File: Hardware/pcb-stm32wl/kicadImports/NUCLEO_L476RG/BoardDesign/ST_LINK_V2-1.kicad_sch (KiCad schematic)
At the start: 70 parts, among them CN1 5075BMR-05-SM, CN5 Header 6X1, CN6 Header 4, T2 9013, U12 STM32F103CBT6, U13 LD3985M33R, X1 8MHz(12pF)

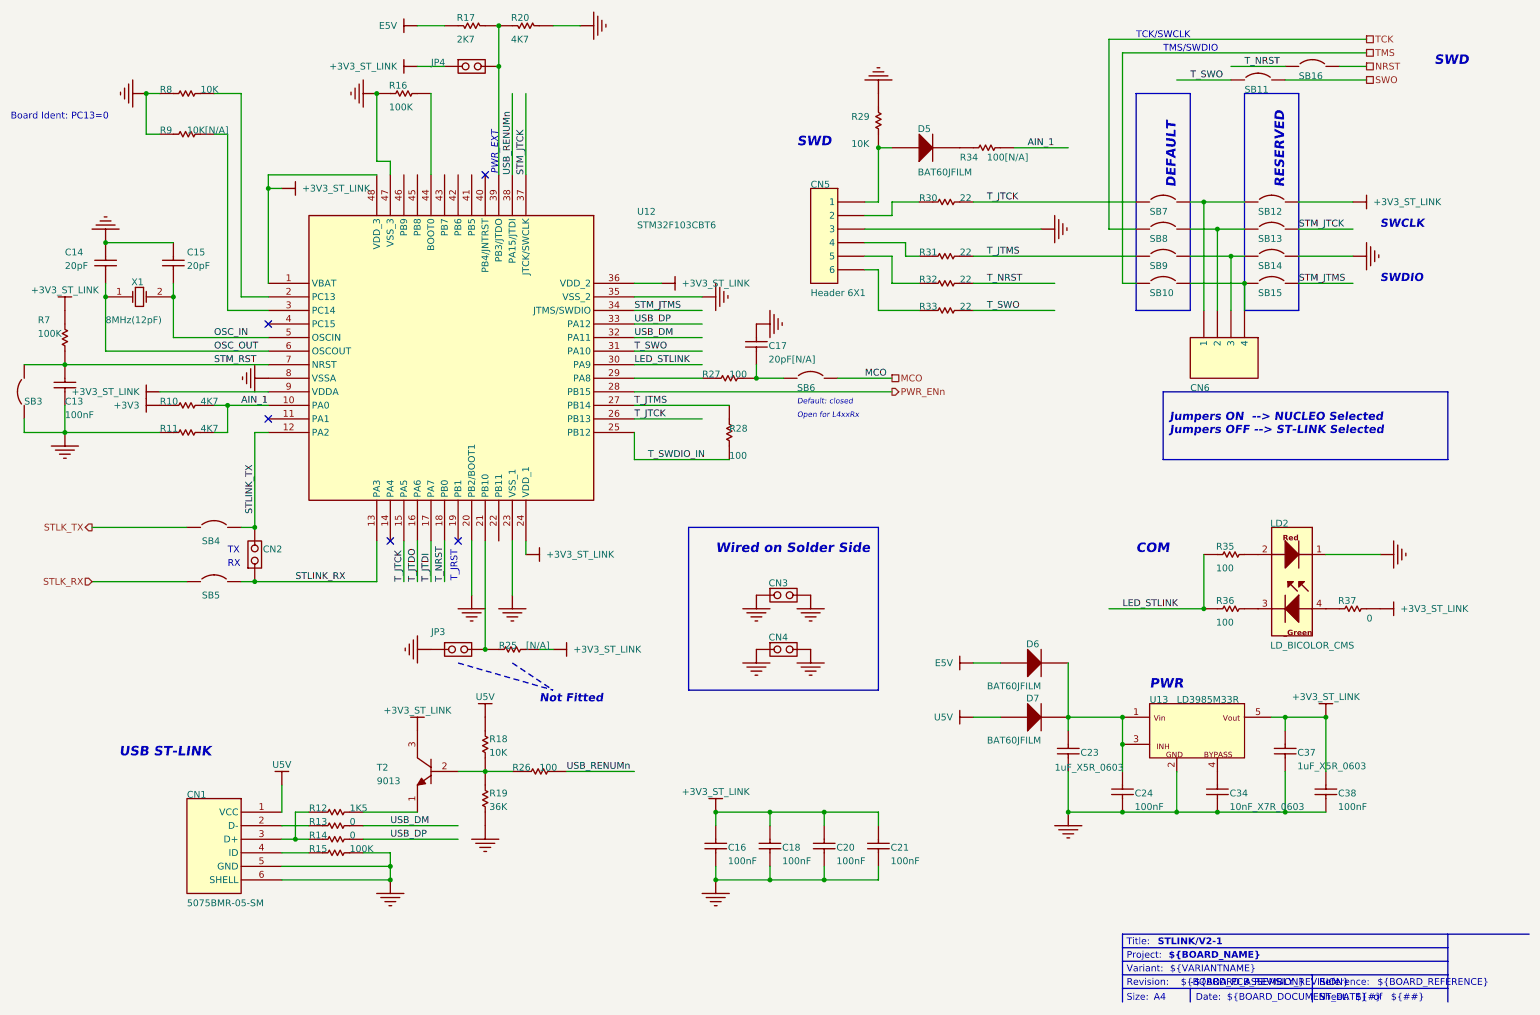
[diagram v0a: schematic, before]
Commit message: . Re-imported NUCLEO_L476RG/BoardDesign/* files using KiCad 9.0.0 one at a time (to avoid a bug evident in misconnections in MCU_64), copied the schematic contents into local kicad_sch files with the same names, prefixed with NUCLEO_L476RG_*
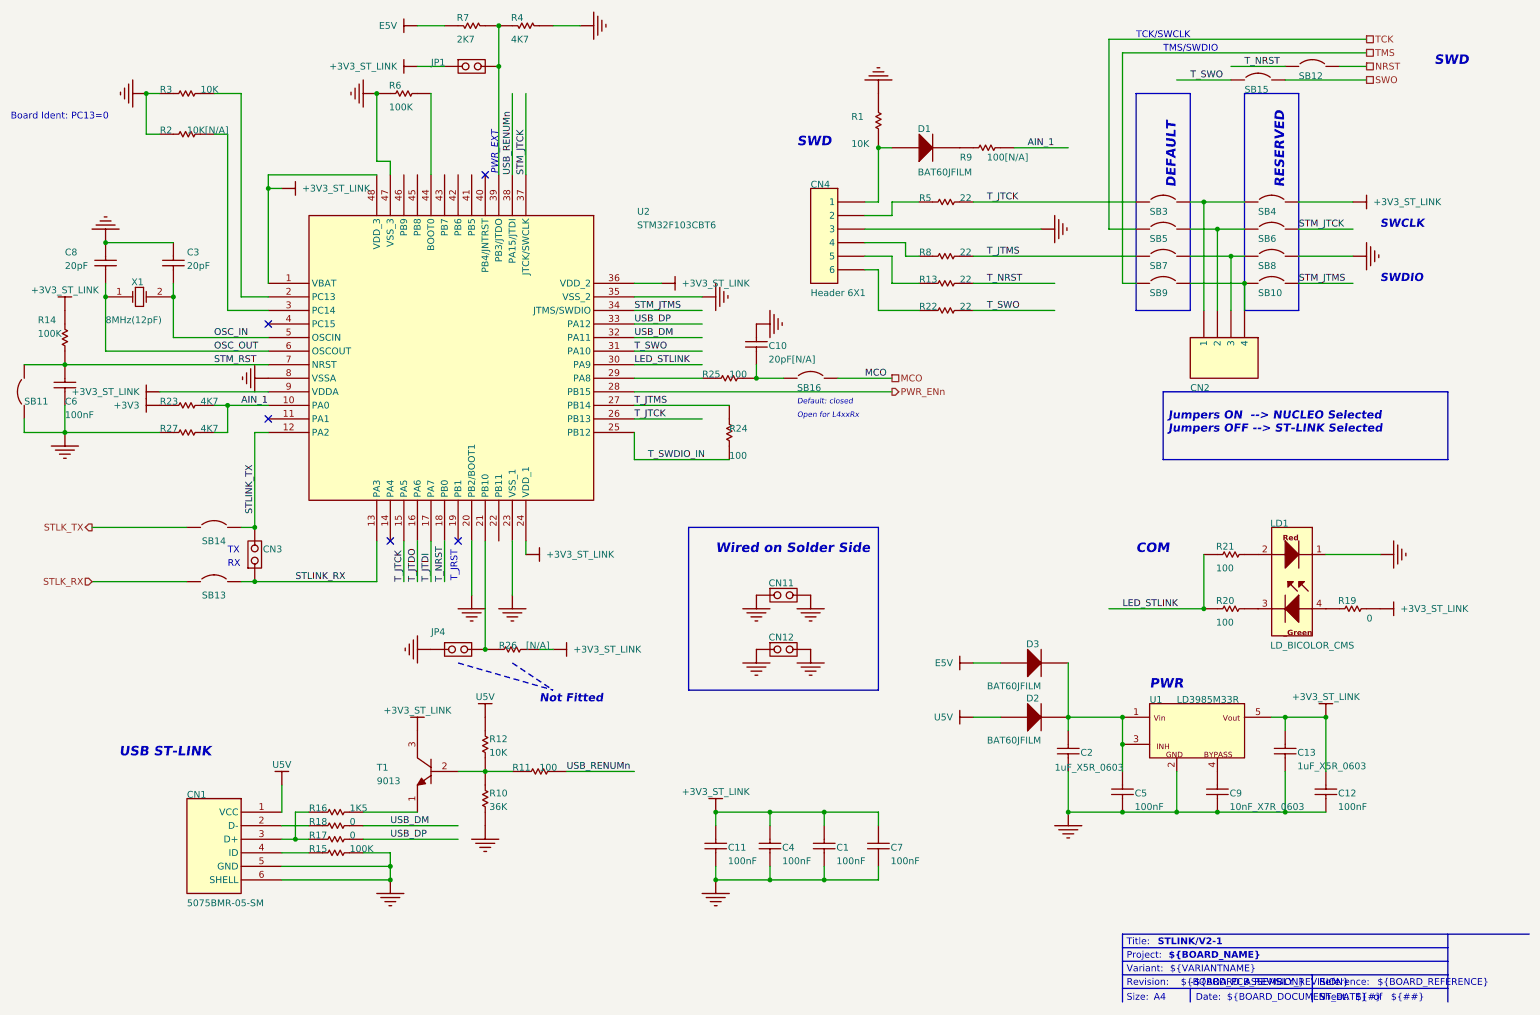
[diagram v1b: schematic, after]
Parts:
- removed C13, C16, C18, C20, C21, C24, C38: 100nF, 0603C, symbol Project_Overview-altium-import:U_ST_LINK_V2-1_1_Capacitor_ST
- removed C14, C15: 20pF, 0603C, symbol Project_Overview-altium-import:U_ST_LINK_V2-1_1_Capacitor_ST
- removed C17: 20pF[N/A], 0603C, symbol Project_Overview-altium-import:U_ST_LINK_V2-1_1_Capacitor_ST
- removed C23: 1uF_X5R_0603, 0603C, symbol Project_Overview-altium-import:U_ST_LINK_V2-1_1_CAP SMD 0603 X5R 1µF 25V 10%
- removed C34: 10nF_X7R_0603, 0603C, symbol Project_Overview-altium-import:U_ST_LINK_V2-1_1_CAP SMD 0603 X7R 10000PF 50V 10%
- removed C37: 1uF_X5R_0603, 0603C, symbol Project_Overview-altium-import:U_ST_LINK_V2-1_3_CAP SMD 0603 X5R 1µF 25V 10%
- removed CN1: 5075BMR-05-SM, USB-MINI-B-SMD, symbol Project_Overview-altium-import:U_ST_LINK_V2-1_0_USB-MINI-typeB connector_0
- removed CN2: ~, SIP2/2.54, symbol Project_Overview-altium-import:U_ST_LINK_V2-1_1_JP2
- removed CN3, CN4, JP3, JP4: ~, SIP2/2.54, symbol Project_Overview-altium-import:U_ST_LINK_V2-1_0_JP2
- removed CN5: Header 6X1, 1*6P, symbol Project_Overview-altium-import:U_ST_LINK_V2-1_0_mirrored_Header 6X1
- removed CN6: Header 4, 1*4, symbol Project_Overview-altium-import:U_ST_LINK_V2-1_3_mirrored_Header 4
- removed D5, D6, D7: BAT60JFILM, SOD323/A, symbol Project_Overview-altium-import:U_ST_LINK_V2-1_0_BAT60JFILM
- removed LD2: LD_BICOLOR_CMS, HSMF-A201, symbol Project_Overview-altium-import:U_ST_LINK_V2-1_0_mirrored_LD_BICOLOR_CMS
- removed R10, R11: 4K7, 0603R, symbol Project_Overview-altium-import:U_ST_LINK_V2-1_0_Res1
- removed R12: 1K5, 0603R, symbol Project_Overview-altium-import:U_ST_LINK_V2-1_0_Res1
- removed R13, R14, R37: 0, 0603R, symbol Project_Overview-altium-import:U_ST_LINK_V2-1_0_Res1
- removed R15, R16: 100K, 0603R, symbol Project_Overview-altium-import:U_ST_LINK_V2-1_0_Res1
- removed R17: 2K7, 0603R, symbol Project_Overview-altium-import:U_ST_LINK_V2-1_0_mirrored_Res1_0
- removed R18: 10K, 0603R, symbol Project_Overview-altium-import:U_ST_LINK_V2-1_1_Res1_0
- removed R19: 36K, 0603R, symbol Project_Overview-altium-import:U_ST_LINK_V2-1_1_Res1_0
- removed R20: 4K7, 0603R, symbol Project_Overview-altium-import:U_ST_LINK_V2-1_0_mirrored_Res1_0
- removed R25: [N/A], 0603R, symbol Project_Overview-altium-import:U_ST_LINK_V2-1_2_Res1_0
- removed R26, R27, R35, R36: 100, 0603R, symbol Project_Overview-altium-import:U_ST_LINK_V2-1_0_Res1
- removed R28: 100, 0603R, symbol Project_Overview-altium-import:U_ST_LINK_V2-1_1_Res1
- removed R29: 10K, 0603R, symbol Project_Overview-altium-import:U_ST_LINK_V2-1_1_Res1
- removed R30, R31, R32, R33: 22, 0603R, symbol Project_Overview-altium-import:U_ST_LINK_V2-1_0_Res1
- removed R34: 100[N/A], 0603R, symbol Project_Overview-altium-import:U_ST_LINK_V2-1_0_Res1
- removed R7: 100K, 0603R, symbol Project_Overview-altium-import:U_ST_LINK_V2-1_1_Res1
- removed R8: 10K, 0603R, symbol Project_Overview-altium-import:U_ST_LINK_V2-1_0_Res1
- removed R9: 10K[N/A], 0603R, symbol Project_Overview-altium-import:U_ST_LINK_V2-1_0_Res1
- removed SB10, SB11, SB12, SB13, SB14, SB15, SB16, SB4, SB5, SB6, SB7, SB8, SB9: Circuit Breaker, JP2_SMD, symbol Project_Overview-altium-import:U_ST_LINK_V2-1_0_Circuit Breaker
- removed SB3: Circuit Breaker, JP2_SMD, symbol Project_Overview-altium-import:U_ST_LINK_V2-1_1_Circuit Breaker
- removed T2: 9013, SOT-23, symbol Project_Overview-altium-import:U_ST_LINK_V2-1_0_mirrored_NPN
- removed U12: STM32F103CBT6, QFP48 7X7, symbol Project_Overview-altium-import:U_ST_LINK_V2-1_0_STM32F103CBT6
- removed U13: LD3985M33R, SOT-23-5L, symbol Project_Overview-altium-import:U_ST_LINK_V2-1_0_LD3985M33R
- removed X1: 8MHz(12pF), XTAL1, symbol Project_Overview-altium-import:U_ST_LINK_V2-1_0_XTAL_0
- added C1, C11, C12, C4, C5, C6, C7: 100nF, 0603C, symbol ST_LINK_V2-1-altium-import:root_1_Capacitor_ST_MCD_TOOLS.SchLib
- added C10: 20pF[N/A], 0603C, symbol ST_LINK_V2-1-altium-import:root_1_Capacitor_ST_MCD_TOOLS.SchLib
- added C13: 1uF_X5R_0603, 0603C, symbol ST_LINK_V2-1-altium-import:root_3_CAP SMD 0603 X5R 1µF 25V 10%_MB963_1.SCHLIB
- added C2: 1uF_X5R_0603, 0603C, symbol ST_LINK_V2-1-altium-import:root_1_CAP SMD 0603 X5R 1µF 25V 10%_MB963_1.SCHLIB
- added C3, C8: 20pF, 0603C, symbol ST_LINK_V2-1-altium-import:root_1_Capacitor_ST_MCD_TOOLS.SchLib
- added C9: 10nF_X7R_0603, 0603C, symbol ST_LINK_V2-1-altium-import:root_1_CAP SMD 0603 X7R 10000PF 50V 10%_MB963_1.SCHL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
- added CN1: 5075BMR-05-SM, USB-MINI-B-SMD, symbol ST_LINK_V2-1-altium-import:root_0_USB-MINI-typeB connector_MCD_TOOLS.SchLib_0
- added CN11, CN12, JP1, JP4: (no value), SIP2/2.54, symbol ST_LINK_V2-1-altium-import:root_0_JP2_*
- added CN2: Header 4, 1*4, symbol ST_LINK_V2-1-altium-import:root_3_mirrored_Header 4_Nucleo_64.SCHLIB
- added CN3: (no value), SIP2/2.54, symbol ST_LINK_V2-1-altium-import:root_1_JP2_MCD_TOOLS.SchLib
- added CN4: Header 6X1, 1*6P, symbol ST_LINK_V2-1-altium-import:root_0_mirrored_Header 6X1_Nucleo_64.SCHLIB
- added D1, D2, D3: BAT60JFILM, SOD323/A, symbol ST_LINK_V2-1-altium-import:root_0_BAT60JFILM_MCD_TOOLS.SchLib
- added LD1: LD_BICOLOR_CMS, HSMF-A201, symbol ST_LINK_V2-1-altium-import:root_0_mirrored_LD_BICOLOR_CMS_MB1136.SCHLIB
- added R1: 10K, 0603R, symbol ST_LINK_V2-1-altium-import:root_1_Res1_Miscellaneous Devices.IntLib
- added R10: 36K, 0603R, symbol ST_LINK_V2-1-altium-import:root_1_Res1_Miscellaneous Devices.IntLib_0
- added R11, R20, R21, R25: 100, 0603R, symbol ST_LINK_V2-1-altium-import:root_0_Res1_Miscellaneous Devices.IntLib
- added R12: 10K, 0603R, symbol ST_LINK_V2-1-altium-import:root_1_Res1_Miscellaneous Devices.IntLib_0
- added R13, R22, R5, R8: 22, 0603R, symbol ST_LINK_V2-1-altium-import:root_0_Res1_Miscellaneous Devices.IntLib
- added R14: 100K, 0603R, symbol ST_LINK_V2-1-altium-import:root_1_Res1_Miscellaneous Devices.IntLib
- added R15, R6: 100K, 0603R, symbol ST_LINK_V2-1-altium-import:root_0_Res1_Miscellaneous Devices.IntLib
- added R16: 1K5, 0603R, symbol ST_LINK_V2-1-altium-import:root_0_Res1_Miscellaneous Devices.IntLib
- added R17, R18, R19: 0, 0603R, symbol ST_LINK_V2-1-altium-import:root_0_Res1_Miscellaneous Devices.IntLib
- added R2: 10K[N/A], 0603R, symbol ST_LINK_V2-1-altium-import:root_0_Res1_Miscellaneous Devices.IntLib
- added R23, R27: 4K7, 0603R, symbol ST_LINK_V2-1-altium-import:root_0_Res1_Miscellaneous Devices.IntLib
- added R24: 100, 0603R, symbol ST_LINK_V2-1-altium-import:root_1_Res1_Miscellaneous Devices.IntLib
- added R26: [N/A], 0603R, symbol ST_LINK_V2-1-altium-import:root_2_Res1_Miscellaneous Devices.IntLib_0
- added R3: 10K, 0603R, symbol ST_LINK_V2-1-altium-import:root_0_Res1_Miscellaneous Devices.IntLib
- added R4: 4K7, 0603R, symbol ST_LINK_V2-1-altium-import:root_0_mirrored_Res1_Miscellaneous Devices.IntLib_0
- added R7: 2K7, 0603R, symbol ST_LINK_V2-1-altium-import:root_0_mirrored_Res1_Miscellaneous Devices.IntLib_0
- added R9: 100[N/A], 0603R, symbol ST_LINK_V2-1-altium-import:root_0_Res1_Miscellaneous Devices.IntLib
- added SB10, SB12, SB3, SB4, SB5, SB6, SB7, SB8, SB9: Circuit Breaker, JP2_SMD, symbol ST_LINK_V2-1-altium-import:root_0_Circuit Breaker_MB915.SCHLIB
- added SB11: Circuit Breaker, JP2_SMD, symbol ST_LINK_V2-1-altium-import:root_1_Circuit Breaker_MB915.SCHLIB
- added SB13, SB14, SB15, SB16: Circuit Breaker, JP2_SMD, symbol ST_LINK_V2-1-altium-import:root_0_Circuit Breaker_MCD_TOOLS.SCHLIB
- added T1: 9013, SOT-23, symbol ST_LINK_V2-1-altium-import:root_0_mirrored_NPN_Miscellaneous Devices.IntLib
- added U1: LD3985M33R, SOT-23-5L, symbol ST_LINK_V2-1-altium-import:root_0_LD3985M33R_MCD_TOOLS.SchLib
- added U2: STM32F103CBT6, QFP48 7X7, symbol ST_LINK_V2-1-altium-import:root_0_STM32F103CBT6_Nucleo_64.SCHLIB
- added X1: 8MHz(12pF), XTAL1, symbol ST_LINK_V2-1-altium-import:root_0_XTAL_MB963_1.SCHLIB_0
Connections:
- net +3V3: now also R23.1
- net +3V3_ST_LINK: now also C1.2, C11.2, C12.2, C13.1, C4.2, C7.2, JP1.1 (COMMON), R14.2, R19.2, R26.1, SB4.2, T1.3 (C), U1.5 (Vout), U2.1 (VBAT), U2.24 (VDD_1), U2.36 (VDD_2), U2.48 (VDD_3), U2.9 (VDDA)
- net AIN_1: now also R23.2, R27.2, R9.2, U2.10 (PA0)
- net E5V: now also D3.1 (A), R7.1
- net GND: now also C1.1, C10.2, C11.1, C12.1, C13.2, C2.1, C3.2, C4.1, C5.1, C6.1, C7.1, C8.2, C9.1, CN1.5 (GND), CN1.6 (SHELL), CN11.1 (COMMON), CN11.2 (NO), CN12.1 (COMMON), CN12.2 (NO), CN4.3, JP4.1 (COMMON), LD1.1, R1.2, R10.1, R15.2, R2.1, R27.1, R3.1, R4.2, R6.1, SB11.1, SB8.2, U1.2 (GND), U2.20 (PB2/BOOT1), U2.23 (VSS_1), U2.35 (VSS_2), U2.47 (VSS_3), U2.8 (VSSA)
- net LED_STLINK: now also R20.1, R21.1, U2.30 (PA9)
- net MCO: now also SB16.2
- net NRST: now also SB12.2
- net OSC_IN: now also C3.1, U2.5 (OSCIN), X1.2 (OSC2)
- net OSC_OUT: now also C8.1, U2.6 (OSCOUT), X1.1 (OSC1)
- net PWR_ENn: now also U2.28 (PB15)
- net STLINK_RX: now also CN3.1 (COMMON), SB13.2, U2.13 (PA3)
- net STLINK_TX: now also CN3.2 (NO), SB14.2, U2.12 (PA2)
- net STLK_RX: now also SB13.1
- net STLK_TX: now also SB14.1
- net STM_JTCK: now also SB6.2, U2.37 (JTCK/SWCLK)
- net STM_JTMS: now also SB10.2, U2.34 (JTMS/SWDIO)
- net STM_RST: now also C6.2, R14.1, SB11.2, U2.7 (NRST)
- net SWO: now also SB15.2
- net TCK: now also SB5.1
- net TMS: now also SB9.1
- net T_JTCK: now also R5.2, SB3.1, U2.15 (PA5), U2.26 (PB13)
- net T_JTDI: now also U2.17 (PA7)
- net T_JTDO: now also U2.16 (PA6)
- net T_JTMS: now also R24.2, R8.2, SB7.1, U2.27 (PB14)
- net T_NRST: now also R13.2, SB12.1, U2.18 (PB0)
- net T_SWDIO_IN: now also R24.1, U2.25 (PB12)
- net T_SWO: now also R22.2, SB15.1, U2.31 (PA10)
- net U5V: now also CN1.1 (VCC), D2.1 (A), R12.2
- net USB_DM: now also R18.2, U2.32 (PA11)
- net USB_DP: now also R17.2, U2.33 (PA12)
- net USB_RENUMn: now also R11.2, U2.38 (PA15/JTDI)
- new net: JP1.2 (NO), R4.1, R7.2, U2.39 (PB3/JTDO)
- new net: CN2.2, SB5.2, SB6.1
- new net: R25.1, U2.29 (PA8)
- new net: C10.1, R25.2, SB16.1
- new net: R6.2, U2.44 (BOOT0)
- new net: CN1.4 (ID), R15.1
- new net: C2.2, C5.2, D2.2 (K), D3.2 (K), U1.1 (Vin), U1.3 (CE)
- new net: C9.2, U1.4 (BYPASS)
- new net: R3.2, U2.2 (PC13)
- new net: CN1.2 (D-), R18.1
- new net: CN2.1, SB3.2, SB4.1
- new net: CN2.4, SB10.1, SB9.2
- new net: R10.2, R11.1, R12.1, T1.2 (B)
- new net: CN4.2, R5.1
- new net: CN4.1, D1.1 (A), R1.1
- new net: CN4.4, R8.1
- new net: CN4.5, R13.1
- new net: CN4.6, R22.1
- new net: LD1.4, R19.1
- new net: D1.2 (K), R9.1
- new net: JP4.2 (NO), R26.2, U2.21 (PB10)
- new net: R2.2, U2.3 (PC14)
- new net: R16.2, T1.1 (E)
- new net: CN1.3 (D+), R16.1, R17.1
- new net: LD1.3, R20.2
- new net: CN2.3, SB7.2, SB8.1
- new net: LD1.2, R21.2
